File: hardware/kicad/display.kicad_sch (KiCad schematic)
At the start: 19 parts, among them J4 687124182122, Q7 SI1308EDL

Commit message: update fottprint
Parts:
- L5: footprint Inductor_SMD:L_Changjiang_FNR4012S -> plantpal:L_Changjiang_FNR4012S
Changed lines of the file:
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@@
       (effects (font (size 1.27 1.27)))
     )
-    (property "Footprint" "Inductor_SMD:L_Changjiang_FNR4012S" (at 160.655 53.975 0)
+    (property "Footprint" "plantpal:L_Changjiang_FNR4012S" (at 160.655 53.975 0)
       (effects (font (size 1.27 1.27)) hide)
     )

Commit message: work in progress
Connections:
- net TSCL: no longer names the net of J4.6 (TSCL)
- net TSDA: no longer names the net of J4.7 (TSDA)
- no-connect marks 1 -> 3
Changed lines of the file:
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@@
   )
   (no_connect (at 46.99 90.805))
+  (no_connect (at 46.99 45.085))
+  (no_connect (at 46.99 41.275))
   (wire (pts (xy 156.21 75.565) (xy 156.21 78.105))
     (stroke (width 0) (type default))
@@
     (stroke (width 0) (type default))
   )
-  (wire (pts (xy 49.53 41.275) (xy 46.99 41.275))
-    (stroke (width 0) (type default))
-  )
   (wire (pts (xy 74.93 33.655) (xy 74.93 38.735))
     (stroke (width 0) (type default))
@@
   )
   (wire (pts (xy 69.85 102.235) (xy 69.85 94.615))
-    (stroke (width 0) (type default))
-  )
-  (wire (pts (xy 49.53 45.085) (xy 46.99 45.085))
     (stroke (width 0) (type default))
   )
@@
     (effects (font (size 1.27 1.27)) (justify left))
   )
-  (hierarchical_label "TSDA" (shape bidirectional) (at 49.53 45.085 0) (fields_autoplaced)
-    (effects (font (size 1.27 1.27)) (justify left))
-  )
-  (hierarchical_label "TSCL" (shape input) (at 49.53 41.275 0) (fields_autoplaced)
-    (effects (font (size 1.27 1.27)) (justify left))
-  )

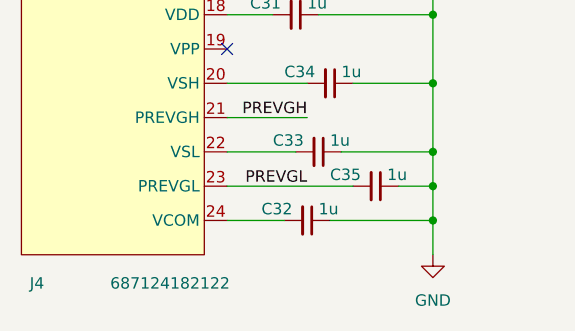
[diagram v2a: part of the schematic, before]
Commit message: change fpc connector
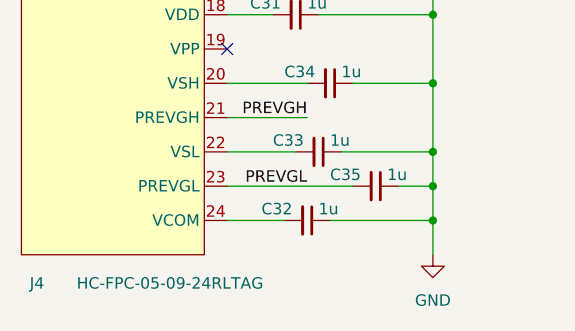
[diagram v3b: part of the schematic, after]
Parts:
- J4: value 687124182122 -> HC-FPC-05-09-24RLTAG; footprint plantpal:687124182122 -> plantpal:FPC-SMD_24P-P0.50_HC-FPC-05-09-24RLTAG; Distributor Mouser -> LCSC; Distributor Link https://www.mouser.com/ProductDetail/Wurth-Elektronik/68712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 -> https://www.lcsc.com/product-detail/FFC-FPC-Connectors_HCTL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; Distributor Part Number 710-687124182122 -> C5213757; Manufacturer Wurth Elektronik -> HCTL; Manufacturer Part Number 687124182122 -> HC-FPC-05-09-24RLTAG; Part Description FFC & FPC Connectors WR-FPC SMT Horiz 0.50mm Dual.Cont. -> FFC & FPC Connectors Clamshell 24P Bottom Contact P=0.5mm
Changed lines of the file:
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@@
       (effects (font (size 1.27 1.27)) (justify left))
     )
-    (property "Value" "687124182122" (at 40.64 116.84 0)
+    (property "Value" "HC-FPC-05-09-24RLTAG" (at 40.64 116.84 0)
       (effects (font (size 1.27 1.27)))
     )
-    (property "Footprint" "plantpal:687124182122" (at 35.56 34.925 0)
+    (property "Footprint" "plantpal:FPC-SMD_24P-P0.50_HC-FPC-05-09-24RLTAG" (at 35.56 34.925 0)
       (effects (font (size 1.27 1.27)) hide)
     )
-    (property "Datasheet" "https://www.we-online.com/catalog/datasheet/687124182122.pdf" (at 35.56 34.925 0)
+    (property "Datasheet" "https://datasheet.lcsc.com/lcsc/2210261730_HCTL-HC-FPC-05-09-24RLTAG_C5213757.pdf" (at 35.56 34.925 0)
       (effects (font (size 1.27 1.27)) hide)
     )
-    (property "Part Description" "FFC & FPC Connectors WR-FPC SMT Horiz 0.50mm Dual.Cont." (at 34.29 62.865 0)
+    (property "Part Description" "FFC & FPC Connectors Clamshell 24P Bottom Contact P=0.5mm" (at 34.29 62.865 0)
       (effects (font (size 1.27 1.27)) hide)
     )
-    (property "Manufacturer" "Wurth Elektronik" (at 34.29 62.865 0)
+    (property "Manufacturer" "HCTL" (at 34.29 62.865 0)
       (effects (font (size 1.27 1.27)) hide)
     )
-    (property "Manufacturer Part Number" "687124182122" (at 34.29 62.865 0)
+    (property "Manufacturer Part Number" "HC-FPC-05-09-24RLTAG" (at 34.29 62.865 0)
       (effects (font (size 1.27 1.27)) hide)
     )
-    (property "Distributor" "Mouser" (at 34.29 62.865 0)
+    (property "Distributor" "LCSC" (at 34.29 62.865 0)
       (effects (font (size 1.27 1.27)) hide)
     )
-    (property "Distributor Part Number" "710-687124182122" (at 34.29 62.865 0)
+    (property "Distributor Part Number" "C5213757" (at 34.29 62.865 0)
       (effects (font (size 1.27 1.27)) hide)
     )
-    (property "Distributor Link" "https://www.mouser.com/ProductDetail/Wurth-Elektronik/687124182122?qs=DvsTirrhYfMkJTUQW4Na4w%3D%3D" (at 34.29 62.865 0)
+    (property "Distributor Link" "https://www.lcsc.com/product-detail/FFC-FPC-Connectors_HCTL-HC-FPC-05-09-24RLTAG_C5213757.html" (at 34.29 62.865 0)
       (effects (font (size 1.27 1.27)) hide)
     )

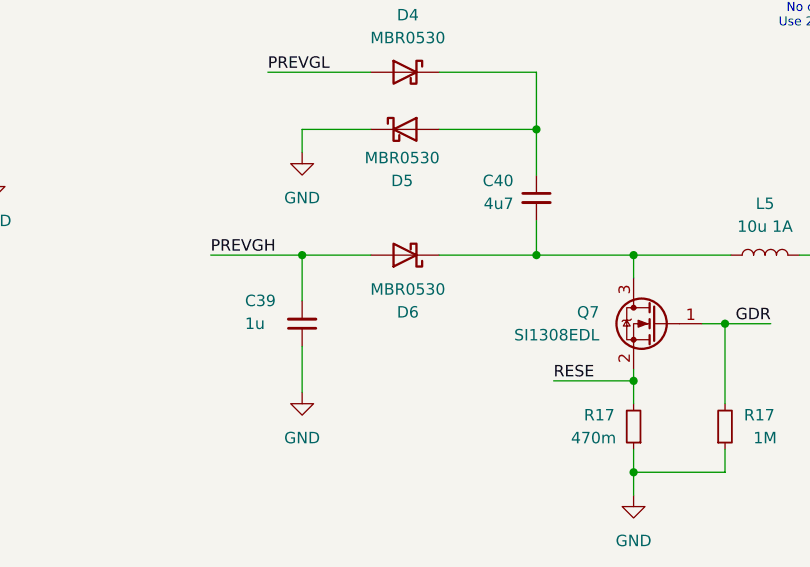
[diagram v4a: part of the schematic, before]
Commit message: fix D6 polarity
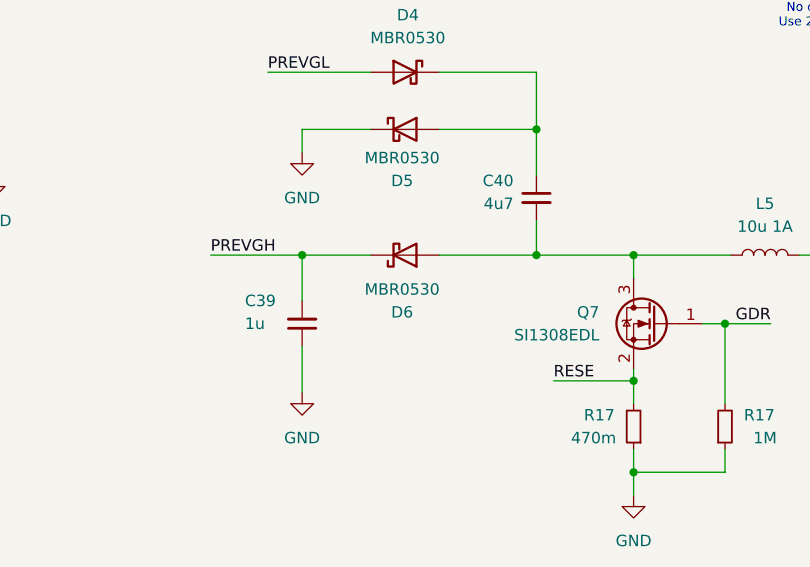
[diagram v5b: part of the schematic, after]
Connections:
- net PREVGH: now also D6.1 (K); no longer D6.2 (A)
- net at C40.2, L5.2, Q7.3 (D): now also D6.2 (A); no longer D6.1 (K)
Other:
- moved on the sheet: D6
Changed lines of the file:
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@@
     )
   )
-  (symbol (lib_id "Diode:MBR0530") (at 120.65 53.975 180) (unit 1)
+  (symbol (lib_id "Diode:MBR0530") (at 120.65 53.975 0) (mirror x) (unit 1)
     (in_bom yes) (on_board yes) (dnp no)
-    (property "Reference" "D6" (at 120.9675 60.325 0)
+    (property "Reference" "D6" (at 120.3325 60.325 0)
       (effects (font (size 1.27 1.27)))
     )
-    (property "Value" "MBR0530" (at 120.9675 57.785 0)
+    (property "Value" "MBR0530" (at 120.3325 57.785 0)
       (effects (font (size 1.27 1.27)))
     )

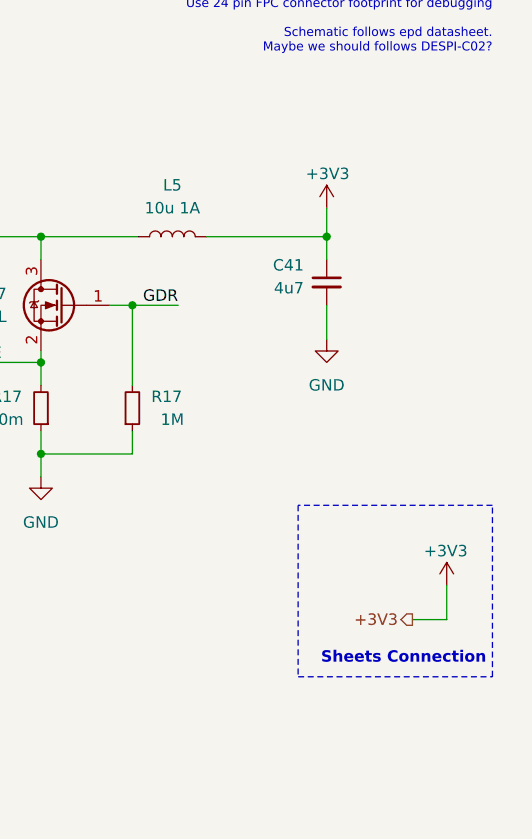
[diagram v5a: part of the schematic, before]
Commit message: re-route sense out, add display power switch
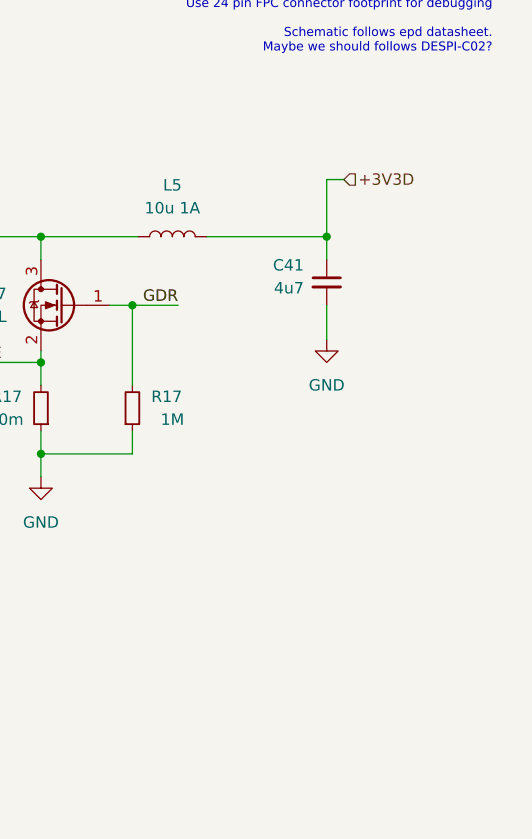
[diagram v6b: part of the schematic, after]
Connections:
- net +3V3: no longer C41.1, L5.1
- new net +3V3D: C41.1, L5.1
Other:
- note removed: "Sheets Connection"

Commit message: fix schematic info
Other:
- company: (none) -> Teapot Laboratories
- title: (none) -> Display
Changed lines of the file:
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@@
   (paper "A5")
   (title_block
-    (date "2023-10-16")
-    (rev "2")
+    (title "Display")
+    (date "2024-01-10")
+    (rev "3")
+    (company "Teapot Laboratories")
   )
   (junction (at 69.85 109.855) (diameter 0) (color 0 0 0 0)

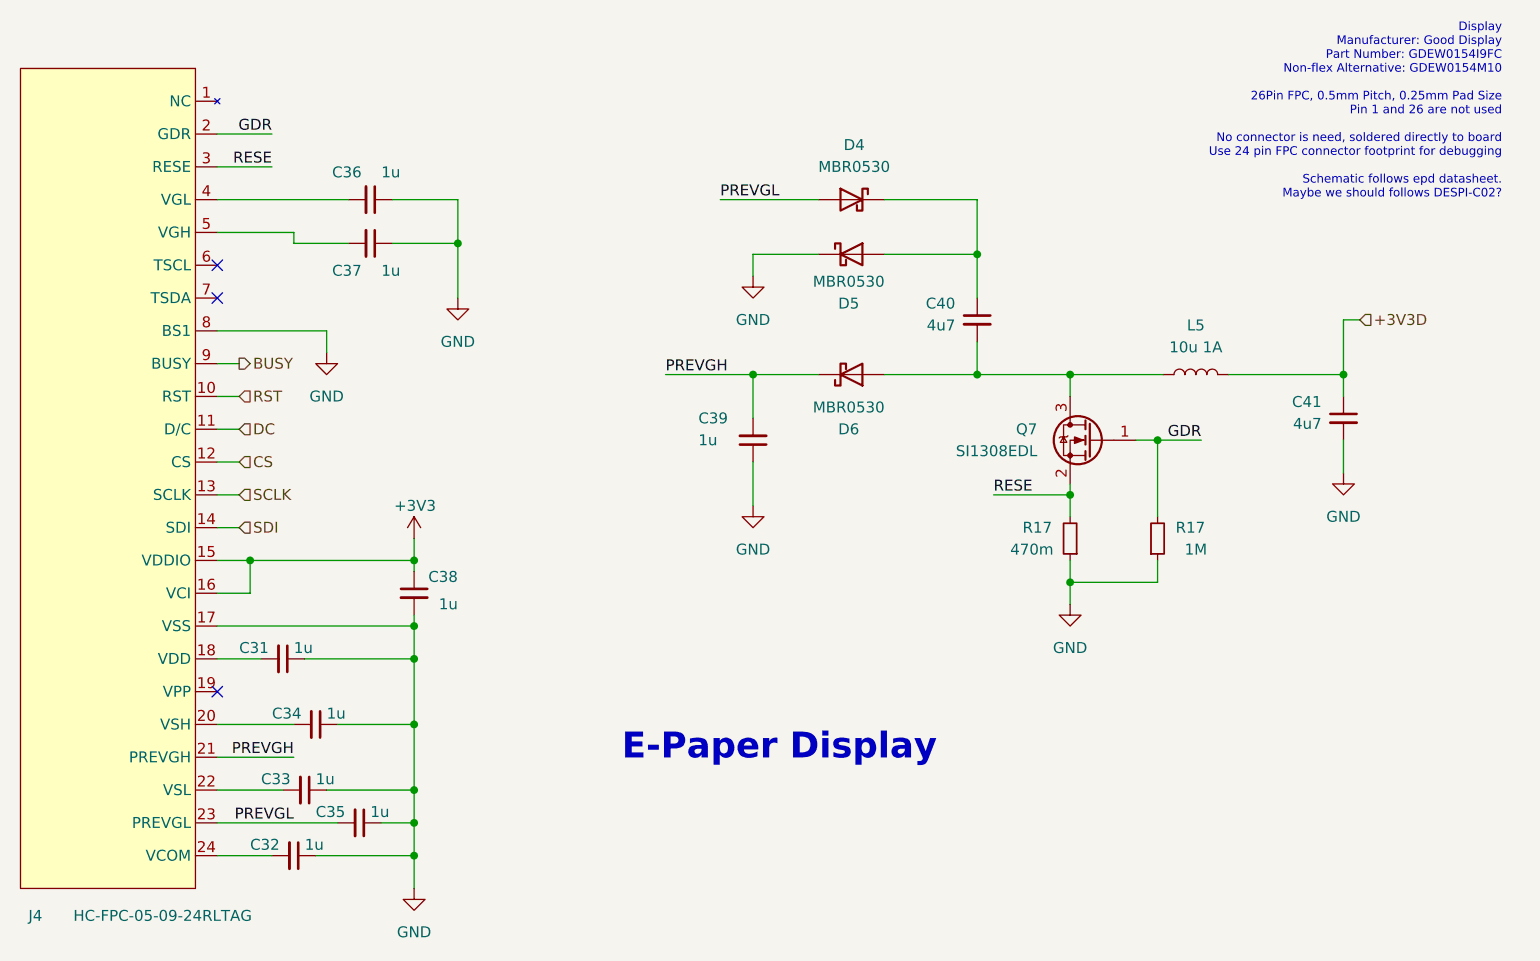
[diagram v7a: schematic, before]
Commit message: re-wire epd power
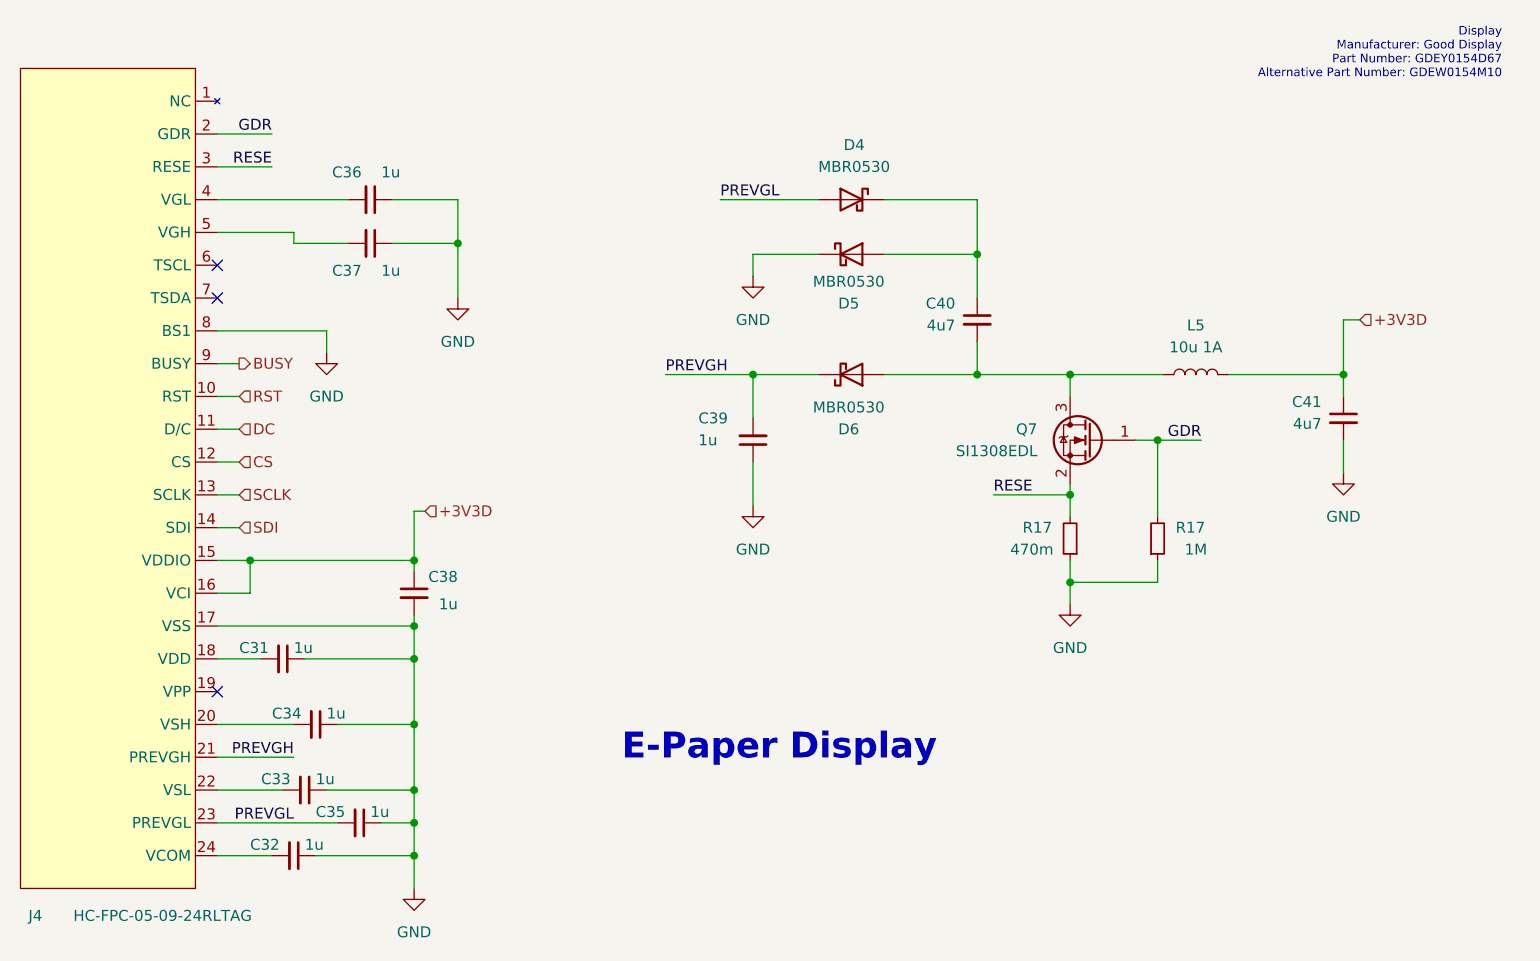
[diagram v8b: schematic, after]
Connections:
- net +3V3 is gone; now on net +3V3D: C38.1, J4.15 (VDDIO), J4.16 (VCI)
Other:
- note added: "Display Manufacturer: Good Display Part Number: GDEY0154D67 Alternative Part Number: GDEW0154M10"
- note removed: "Display Manufacturer: Good Display Part Number: GDEW0154I9FC Non-flex Alternative: GDEW0154M10 26Pin FPC, 0.5mm Pitch, 0.25mm Pad Size Pin 1 and 26 are not used No connector is need, soldered directly to board Use 24 pin FPC connector footprint for debugging Schematic follows epd datasheet. Maybe we should follows DESPI-C02?"
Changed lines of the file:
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@@
   (title_block
     (title "Display")
-    (date "2024-01-10")
-    (rev "3")
+    (date "2024-02-01")
+    (rev "4")
     (company "Teapot Laboratories")
   )
@@
     (stroke (width 0) (type default))
   )
-  (wire (pts (xy 69.85 73.025) (xy 69.85 75.565))
+  (wire (pts (xy 69.85 69.85) (xy 69.85 75.565))
     (stroke (width 0) (type default))
   )
@@
     (stroke (width 0) (type default))
   )
+  (wire (pts (xy 69.85 69.85) (xy 71.12 69.85))
+    (stroke (width 0) (type default))
+  )
   (wire (pts (xy 55.88 94.615) (xy 46.99 94.615))
     (stroke (width 0) (type default))
@@
     (stroke (width 0) (type default))
   )
-  (text "Display \nManufacturer: Good Display\nPart Number: GDEW0154I9FC\nNon-flex Alternative: GDEW0154M10\n\n26Pin FPC, 0.5mm Pitch, 0.25mm Pad Size\nPin 1 and 26 are not used \n\nNo connector is need, soldered directly to board\nUse 24 pin FPC connector footprint for debugging\n\nSchematic follows epd datasheet.\nMaybe we should follows DESPI-C02?"
-    (at 196.215 33.655 0)
+  (text "Display \nManufacturer: Good Display\nPart Number: GDEY0154D67\nAlternative Part Number: GDEW0154M10"
+    (at 196.215 19.685 0)
     (effects (font (size 1 1)) (justify right bottom))
   )
@@
   )
   (hierarchical_label "DC" (shape input) (at 49.53 60.325 0) (fields_autoplaced)
+    (effects (font (size 1.27 1.27)) (justify left))
+  )
+  (hierarchical_label "+3V3D" (shape input) (at 71.12 69.85 0) (fields_autoplaced)
     (effects (font (size 1.27 1.27)) (justify left))
   )
@@
         )
       )
-    )
-  )
-  (symbol (lib_id "power:+3V3") (at 69.85 73.025 0) (unit 1)
-    (in_bom yes) (on_board yes) (dnp no)
-    (property "Reference" "#PWR049" (at 69.85 76.835 0)
-      (effects (font (size 1.27 1.27)) hide)
-    )
-    (property "Value" "+3V3" (at 72.39 69.215 0)
-      (effects (font (size 1.27 1.27)) (justify right))
-    )
-    (property "Footprint" "" (at 69.85 73.025 0)
-      (effects (font (size 1.27 1.27)) hide)
-    )
-    (property "Datasheet" "" (at 69.85 73.025 0)
-      (effects (font (size 1.27 1.27)) hide)
-    )
-    (pin "1")
-    (instances
-      (project "plantpal"
-        (path "/59b4123e-c7be-466b-a5db-658b8f0c1171"
-          (reference "#PWR049") (unit 1)
-        )
-        (path "/59b4123e-c7be-466b-a5db-658b8f0c1171/0bc89df9-c404-42cc-aab4-4237df7294d4"
-          (reference "#PWR086") (unit 1)
-        )
-        (path "/59b4123e-c7be-466b-a5db-658b8f0c1171/416559aa-55f3-4db2-bf13-04c2bb6b0caa"
-          (reference "#PWR091") (unit 1)
-        )
-        (path "/59b4123e-c7be-466b-a5db-658b8f0c1171/943ab7c0-d00c-4ea0-8716-990ca6b0cb6f"
-          (reference "#PWR089") (unit 1)
-        )
-        (path "/59b4123e-c7be-466b-a5db-658b8f0c1171/3265fc00-478b-4188-a908-4fc9b1aaf6ab"
-          (reference "#PWR093") (unit 1)
-        )
-      )
-      (project "bwlr1e"
-        (path "/630c8da6-5464-4eef-824d-89618087f4b4"
-          (reference "#PWR0134") (unit 1)
-        )
-      )
